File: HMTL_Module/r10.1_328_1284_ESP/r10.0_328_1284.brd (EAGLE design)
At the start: 80 x 60 mm, 43 parts, among them U2 ATMEGA328P_PDIP, Y1 16MHz

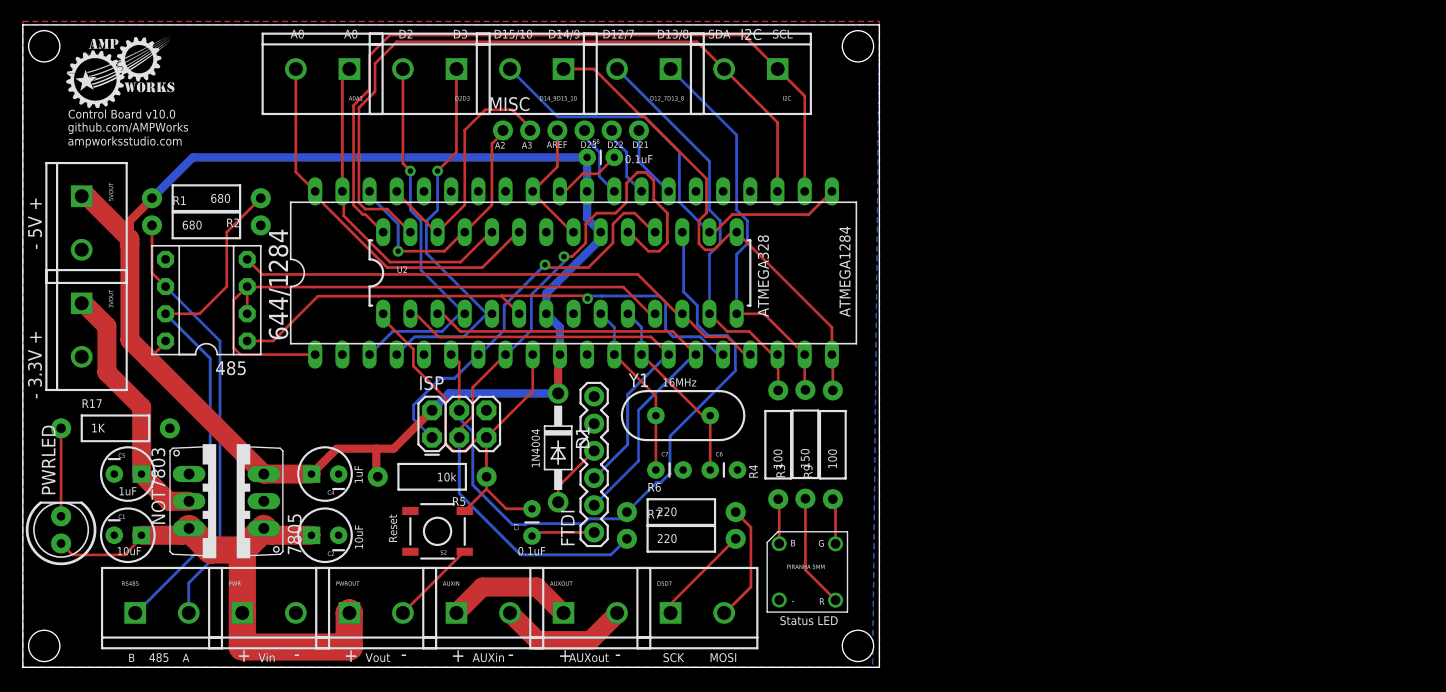
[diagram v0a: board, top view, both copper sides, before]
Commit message: Added the ESP8266 module to r10.0_328_1284
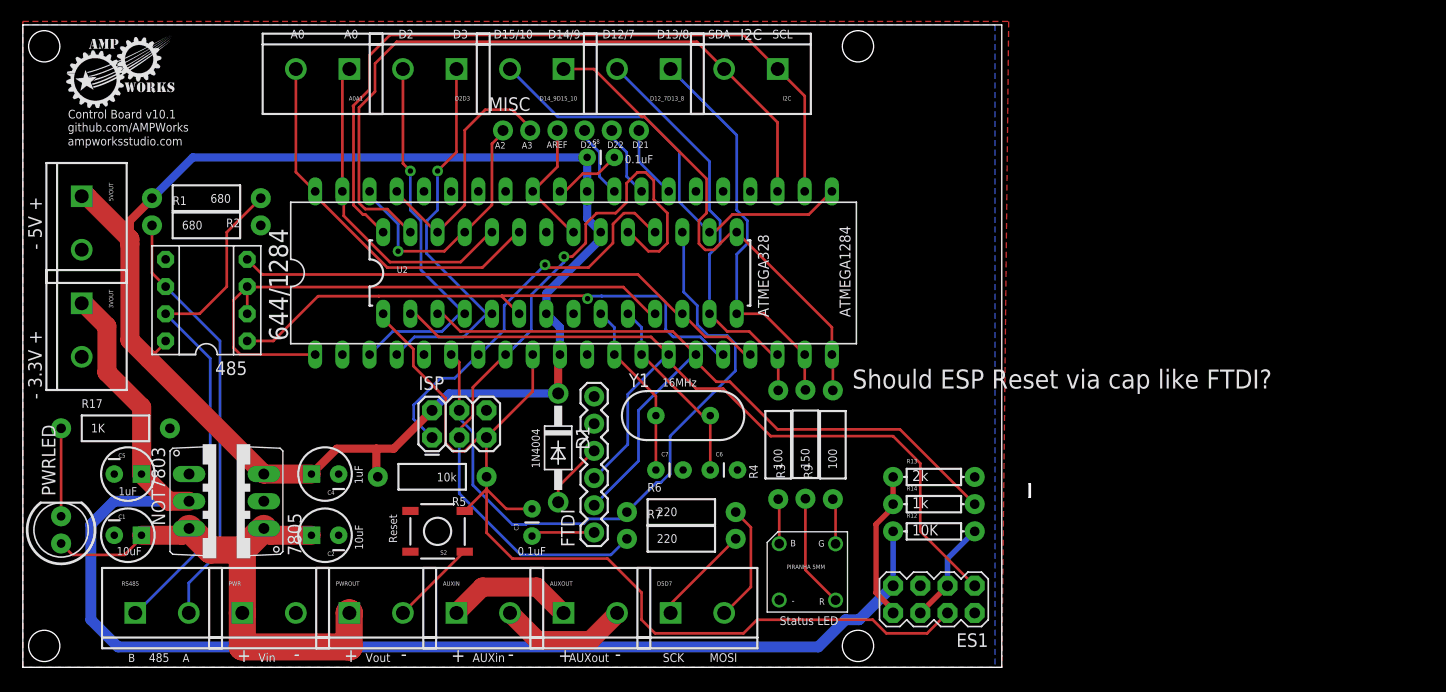
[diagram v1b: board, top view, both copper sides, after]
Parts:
- added ES1: (no value), SparkFun-Connectors:2X4
- added R12: 10K, SparkFun-Resistors:AXIAL-0.3
- added R13: 2k, SparkFun-Resistors:AXIAL-0.3
- added R14: 1k, SparkFun-Resistors:AXIAL-0.3
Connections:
- net VCC renamed 5V
- removed net 3VVCC: 3VOUT.1, C5.1, NOT7803.2
- new net 3.3V: 3VOUT.1, C5.1, ES1.7, NOT7803.2, R12.P$1
- new net CH_PD: ES1.3, ES1.6, R12.P$2
- new net ESP_RST: ES1.5
- new net ESP_TX: ES1.8, R13.P$1, R14.P$1
- net GND: now also ES1.2, R13.P$2
- net RESET: now also ES1.4
- net RX: now also ES1.1
- net TX: now also R14.P$2
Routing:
- net 3.3V: track 0.00 -> 129.0 mm
- net RESET: track 41.4 -> 95.7 mm
- net RX: track 40.2 -> 81.8 mm
- net TX: track 43.8 -> 76.0 mm
- net 3VVCC: track 23.9 -> 0.00 mm
- net ESP_TX: track 0.00 -> 14.0 mm
- net CH_PD: track 0.00 -> 9.72 mm
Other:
- board size 80 x 60 mm -> 94.1 x 60 mm
- board text added: "Control Board v10.1"
- board text added: "Should ESP Reset via cap like FTDI?"
- board text removed: "Control Board v10.0"
